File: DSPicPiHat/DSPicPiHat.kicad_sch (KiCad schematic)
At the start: 85 parts, among them J1 Conn_01x09_Female, J2 Conn_01x04_Female, J4 Conn_PIC_ICSP_ICD, J5 USB_C_Receptacle_USB2.0, J6 PowerInput, J8 RasPiHeaders, SW1 POWER_Select, SW2 SW_DIP_x08, U1 DSPIC33CH512MP508T-I_PT, U10 DF5A6.2CJE_LM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

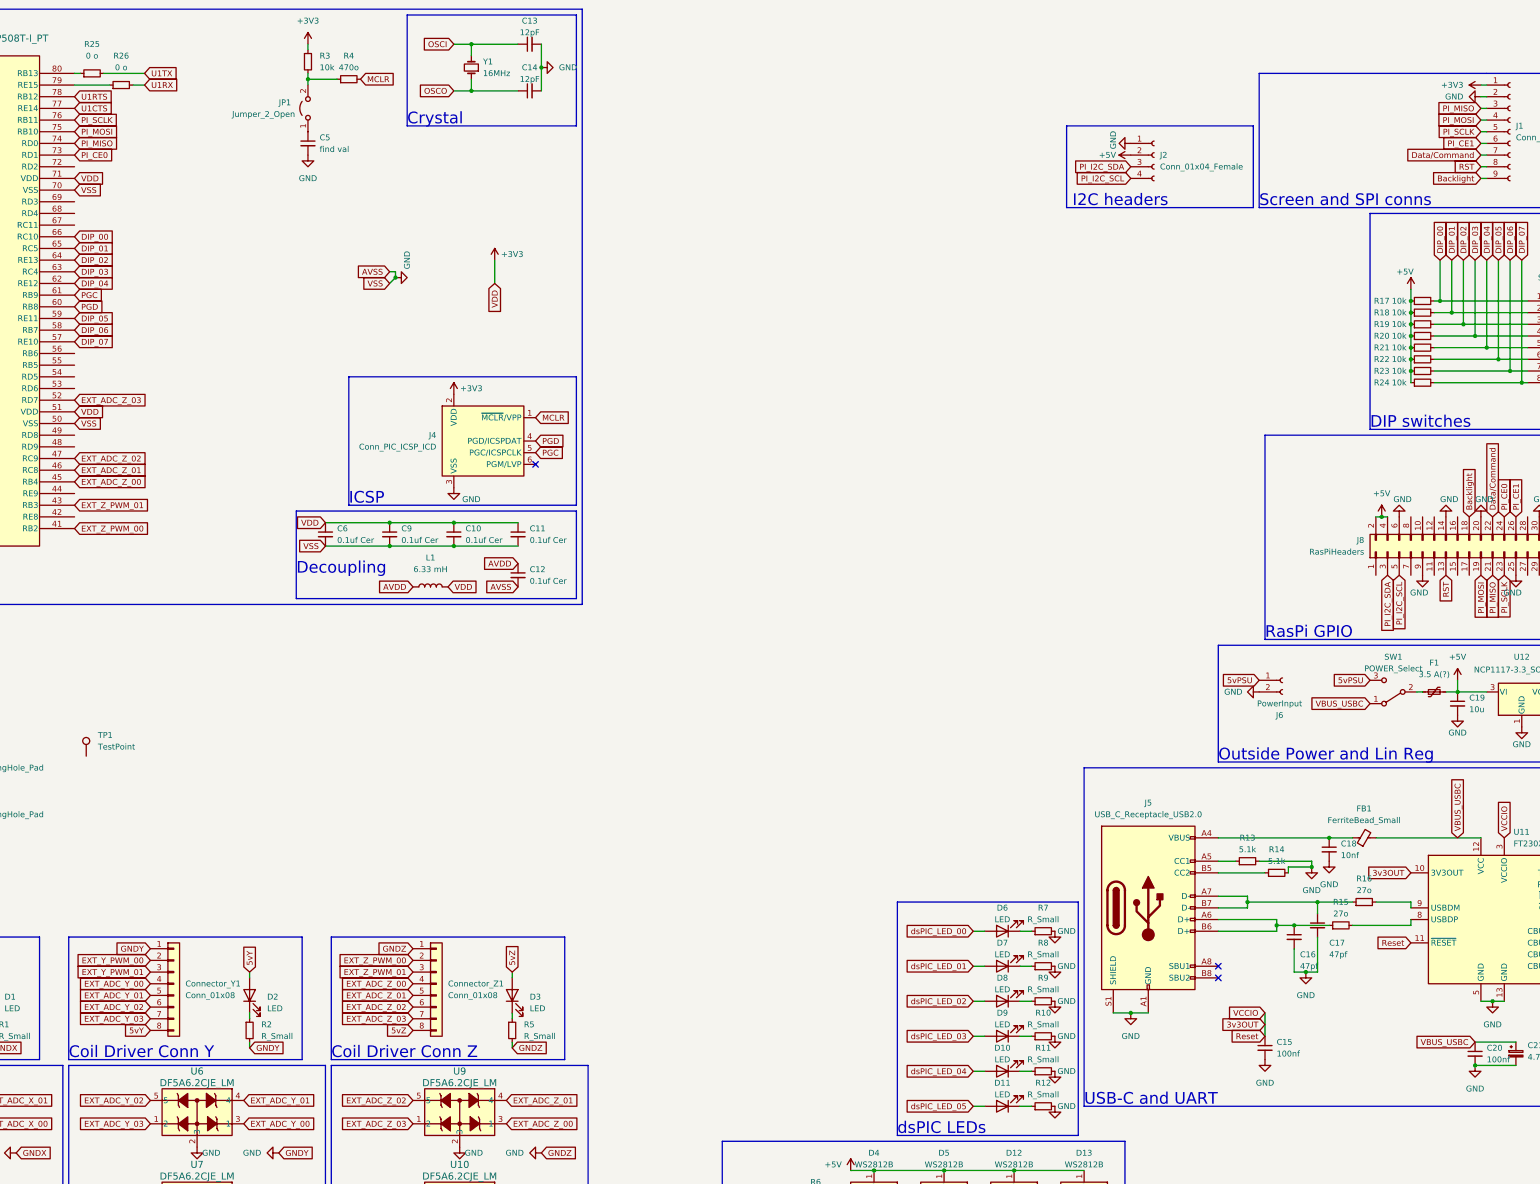
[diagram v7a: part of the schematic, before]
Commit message: filling in unkown values and footprints
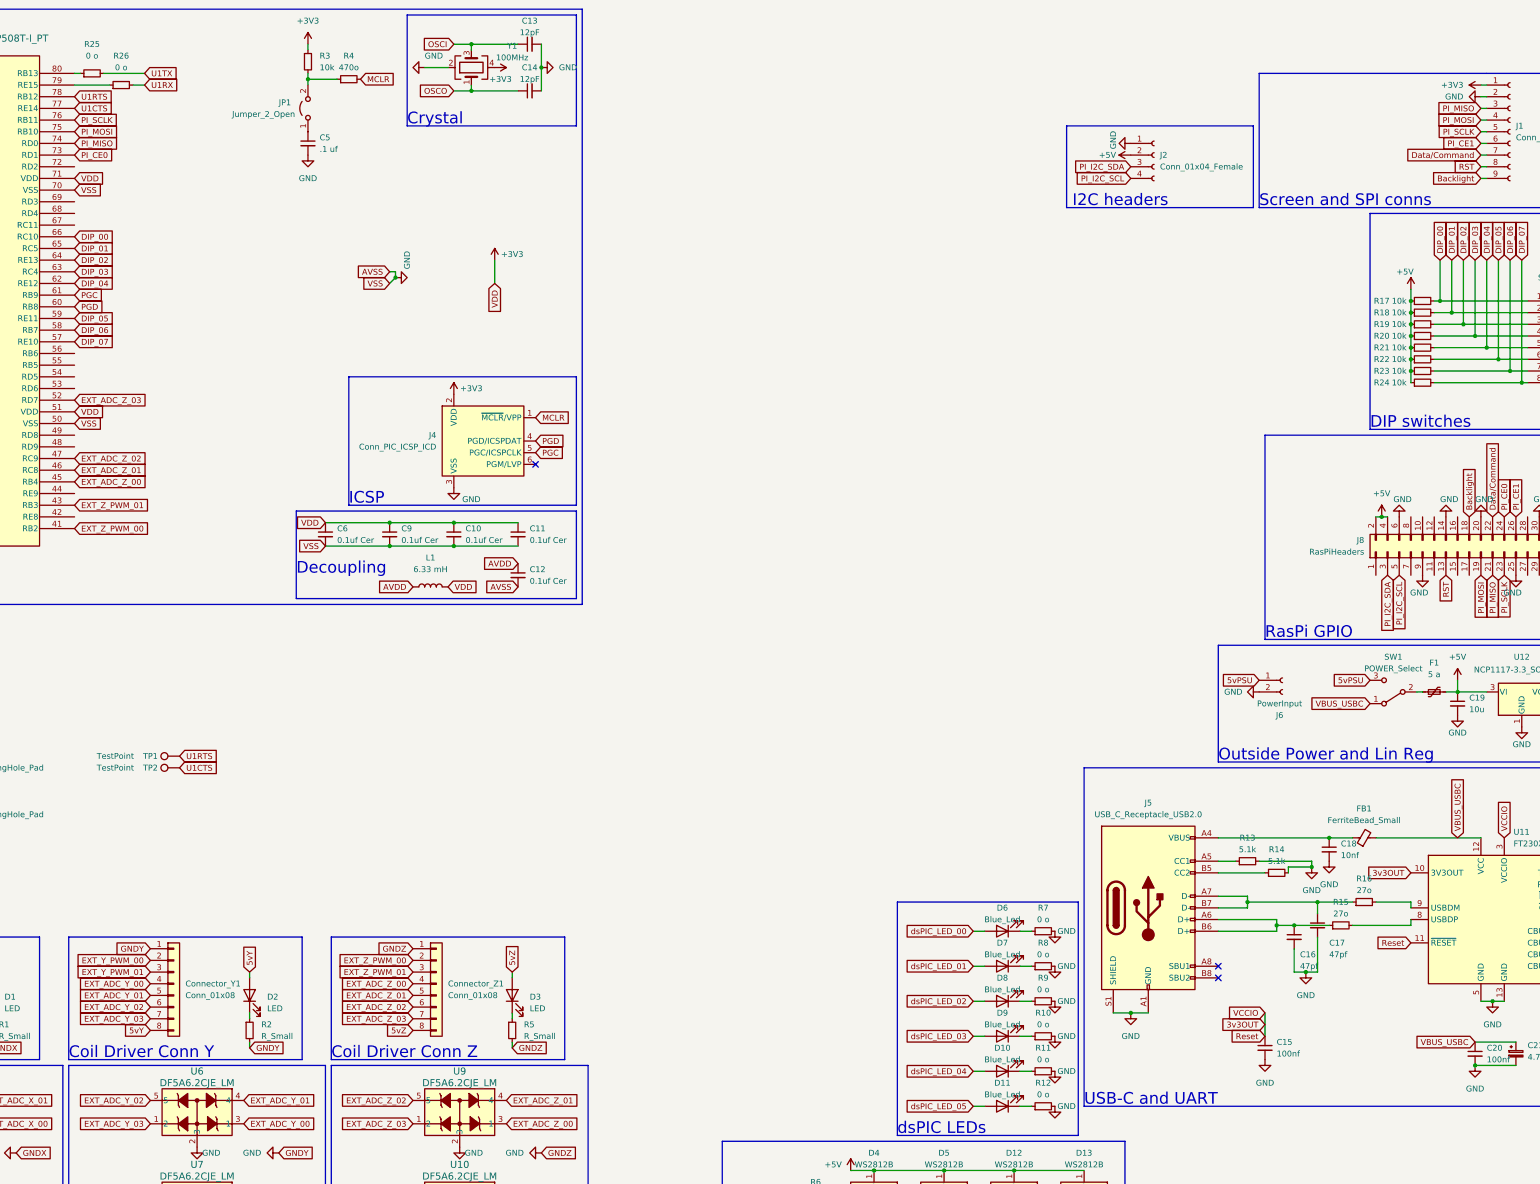
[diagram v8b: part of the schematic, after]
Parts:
- removed Y1: 16MHz, Crystal:Crystal_SMD_Abracon_ABM10-4Pin_2.5x2.0mm, symbol Device:Crystal_Small
- added TP2: TestPoint, TestPoint:TestPoint_Pad_D1.0mm, symbol Connector:TestPoint
- added Y1: 100MHz, Crystal:Crystal_SMD_2520-4Pin_2.5x2.0mm, symbol Device:Crystal_GND24
- C5: value find val -> .1 uf
- D10, D11, D6, D7, D8, D9: value LED -> Blue_Led
- F1: value 3.5 A(?) -> 5 a; footprint Fuse:Fuse_2920_7451Metric -> Fuse:Fuse_1210_3225Metric
- R10, R11, R12, R7, R8, R9: value R_Small -> 0 o
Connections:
- net +3V3: now also Y1.4
- net GND: now also Y1.2
- net OSCI: now also Y1.3
- net OSCO: now also Y1.1
- net U1CTS: now also TP2.1
- net U1RTS: now also TP1.1
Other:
- moved on the sheet: TP1
